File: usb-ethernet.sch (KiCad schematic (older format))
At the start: 17 parts

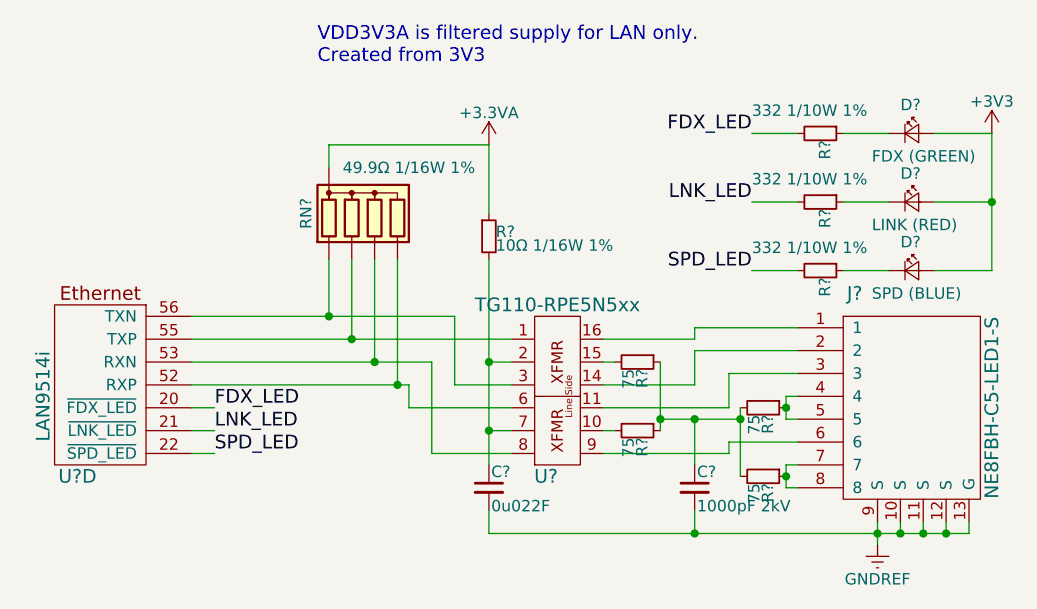
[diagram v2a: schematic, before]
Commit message: Updated footprint assignments
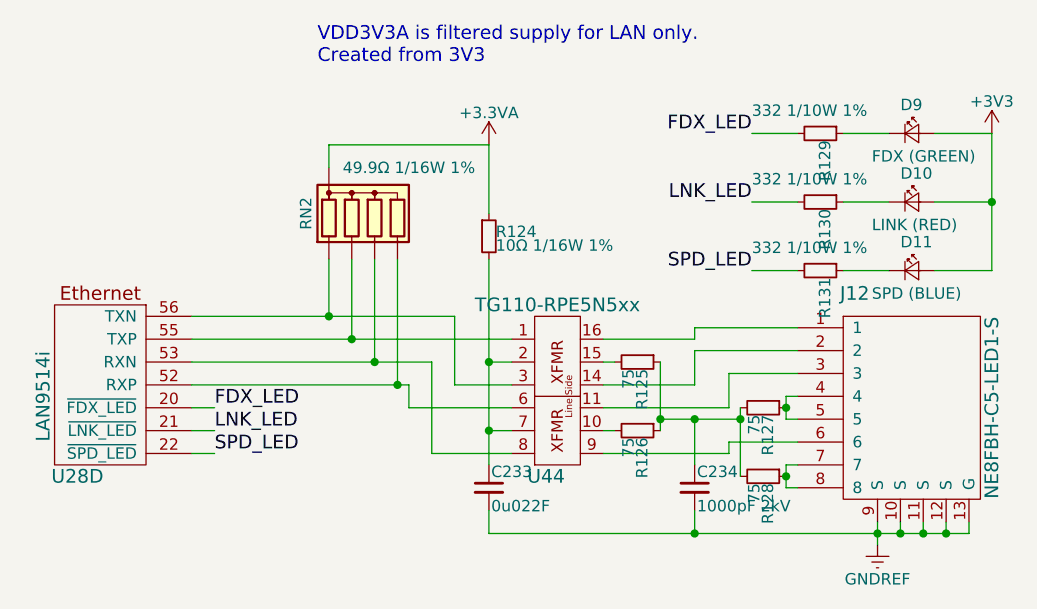
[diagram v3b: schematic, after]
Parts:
- C233, C234: renamed from C?; footprint Capacitors_SMD:C_0603_HandSoldering -> Capacitors_SMD:C_0603
- D10, D11, D9: renamed from D?; footprint (none) -> LEDs:LED_0603
- R124, R125, R126, R127, R128, R129, R130, R131: renamed from R?; footprint Capacitors_SMD:C_0603_HandSoldering -> Resistors_SMD:R_0603
- gave numbers to parts that had none: 4
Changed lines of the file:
@@
 P 3550 3750
 AR Path="/58DEDA35/5903ABC9" Ref="U?"  Part="4"
-AR Path="/58DEDA35/5903AB75/5903ABC9" Ref="U?"  Part="4"
-F 0 "U?" H 3650 3350 60  0000 C CNN
+AR Path="/58DEDA35/5903AB75/5903ABC9" Ref="U28"  Part="4"
+F 0 "U28" H 3650 3350 60  0000 C CNN
 F 1 "LAN9514i" V 3800 3700 60  0000 C CNN
 F 2 "Housings_DFN_QFN:QFN-64-1EP_9x9mm_Pitch0.5mm" H 4250 4250 60  0001 C CNN
@@
 $EndComp
 $Comp
-L TG110-RPE5N5xx U?
+L TG110-RPE5N5xx U44
 U 1 1 590032EB
 P 5550 3800
-F 0 "U?" H 5500 4150 60  0000 C CNN
+F 0 "U44" H 5500 4150 60  0000 C CNN
 F 1 "TG110-RPE5N5xx" H 5550 3400 60  0000 C CNN
 F 2 "" H 5050 4000 60  0001 C CNN
@@
 $EndComp
 $Comp
-L NE8FBH-C5-LED1-S J?
+L NE8FBH-C5-LED1-S J12
 U 1 1 5900332E
 P 7100 3800
-F 0 "J?" H 6850 4250 60  0000 C CNN
+F 0 "J12" H 6850 4250 60  0000 C CNN
 F 1 "NE8FBH-C5-LED1-S" V 7450 3750 60  0000 C CNN
 F 2 "" H 7000 3700 60  0001 C CNN
@@
 $EndComp
 $Comp
-L R_Small R?
+L R_Small R125
 U 1 1 5900376D
 P 5900 3650
-F 0 "R?" H 5930 3670 50  0000 L CNN
+F 0 "R125" H 5930 3670 50  0000 L CNN
 F 1 "75" H 5930 3610 50  0000 L CNN
-F 2 "Capacitors_SMD:C_0603_HandSoldering" H 5900 3650 50  0001 C CNN
+F 2 "Resistors_SMD:R_0603" H 5900 3650 50  0001 C CNN
 F 3 "" H 5900 3650 50  0001 C CNN
 	1    5900 3650
@@
 $EndComp
 $Comp
-L R_Small R?
+L R_Small R126
 U 1 1 590037C5
 P 5900 3950
-F 0 "R?" H 5930 3970 50  0000 L CNN
+F 0 "R126" H 5930 3970 50  0000 L CNN
 F 1 "75" H 5930 3910 50  0000 L CNN
-F 2 "Capacitors_SMD:C_0603_HandSoldering" H 5900 3950 50  0001 C CNN
+F 2 "Resistors_SMD:R_0603" H 5900 3950 50  0001 C CNN
 F 3 "" H 5900 3950 50  0001 C CNN
 	1    5900 3950
@@
 $EndComp
 $Comp
-L R_Small R?
+L R_Small R127
 U 1 1 5900382C
 P 6450 3850
-F 0 "R?" H 6480 3870 50  0000 L CNN
+F 0 "R127" H 6480 3870 50  0000 L CNN
 F 1 "75" H 6480 3810 50  0000 L CNN
-F 2 "Capacitors_SMD:C_0603_HandSoldering" H 6450 3850 50  0001 C CNN
+F 2 "Resistors_SMD:R_0603" H 6450 3850 50  0001 C CNN
 F 3 "" H 6450 3850 50  0001 C CNN
 	1    6450 3850
@@
 $EndComp
 $Comp
-L R_Small R?
+L R_Small R128
 U 1 1 59003855
 P 6450 4150
-F 0 "R?" H 6480 4170 50  0000 L CNN
+F 0 "R128" H 6480 4170 50  0000 L CNN
 F 1 "75" H 6480 4110 50  0000 L CNN
-F 2 "Capacitors_SMD:C_0603_HandSoldering" H 6450 4150 50  0001 C CNN
+F 2 "Resistors_SMD:R_0603" H 6450 4150 50  0001 C CNN
 F 3 "" H 6450 4150 50  0001 C CNN
 	1    6450 4150
@@
 $EndComp
 $Comp
-L C_Small C?
+L C_Small C234
 U 1 1 5900394D
 P 6150 4200
-F 0 "C?" H 6160 4270 50  0000 L CNN
+F 0 "C234" H 6160 4270 50  0000 L CNN
 F 1 "1000pF 2kV" H 6160 4120 50  0000 L CNN
-F 2 "Capacitors_SMD:C_0603_HandSoldering" H 6150 4200 50  0001 C CNN
+F 2 "Capacitors_SMD:C_0603" H 6150 4200 50  0001 C CNN
 F 3 "" H 6150 4200 50  0001 C CNN
 F 4 "0.00@0" H 6150 4200 60  0001 C CNN "Pricing"
@@
 $EndComp
 $Comp
-L GNDREF #PWR?
+L GNDREF #PWR0185
 U 1 1 59003AB4
 P 6950 4450
-F 0 "#PWR?" H 6950 4200 50  0001 C CNN
+F 0 "#PWR0185" H 6950 4200 50  0001 C CNN
 F 1 "GNDREF" H 6950 4300 50  0000 C CNN
 F 2 "" H 6950 4450 50  0001 C CNN
@@
 $EndComp
 $Comp
-L R_Small R?
+L R_Small R124
 U 1 1 59003EAC
 P 5250 3100
-F 0 "R?" H 5280 3120 50  0000 L CNN
+F 0 "R124" H 5280 3120 50  0000 L CNN
 F 1 "10Ω 1/16W 1%" H 5280 3060 50  0000 L CNN
-F 2 "Capacitors_SMD:C_0603_HandSoldering" H 5250 3100 50  0001 C CNN
+F 2 "Resistors_SMD:R_0603" H 5250 3100 50  0001 C CNN
 F 3 "" H 5250 3100 50  0001 C CNN
 F 4 "0.00@0" H 5250 3100 60  0001 C CNN "Pricing"
@@
 $EndComp
 $Comp
-L R_Network04 RN?
+L R_Network04 RN2
 U 1 1 5900455A
 P 4750 3000
-F 0 "RN?" V 4450 3000 50  0000 C CNN
+F 0 "RN2" V 4450 3000 50  0000 C CNN
 F 1 "49.9Ω 1/16W 1%" H 4900 3200 50  0000 C CNN
 F 2 "Resistors_THT:R_Array_SIP5" V 5025 3000 50  0001 C CNN
@@
 $EndComp
 $Comp
-L LED_Small D?
+L LED_Small D10
 U 1 1 59005A5F
 P 7100 2950
-F 0 "D?" H 7050 3075 50  0000 L CNN
+F 0 "D10" H 7050 3075 50  0000 L CNN
 F 1 "LINK (RED)" H 6925 2850 50  0000 L CNN
-F 2 "" V 7100 2950 50  0001 C CNN
+F 2 "LEDs:LED_0603" V 7100 2950 50  0001 C CNN
 F 3 "" V 7100 2950 50  0001 C CNN
 	1    7100 2950
@@
 $EndComp
 $Comp
-L LED_Small D?
+L LED_Small D11
 U 1 1 59005AF2
 P 7100 3250
-F 0 "D?" H 7050 3375 50  0000 L CNN
+F 0 "D11" H 7050 3375 50  0000 L CNN
 F 1 "SPD (BLUE)" H 6925 3150 50  0000 L CNN
-F 2 "" V 7100 3250 50  0001 C CNN
+F 2 "LEDs:LED_0603" V 7100 3250 50  0001 C CNN
 F 3 "" V 7100 3250 50  0001 C CNN
 	1    7100 3250
@@
 $EndComp
 $Comp
-L LED_Small D?
+L LED_Small D9
 U 1 1 59005B83
 P 7100 2650
-F 0 "D?" H 7050 2775 50  0000 L CNN
+F 0 "D9" H 7050 2775 50  0000 L CNN
 F 1 "FDX (GREEN)" H 6925 2550 50  0000 L CNN
-F 2 "" V 7100 2650 50  0001 C CNN
+F 2 "LEDs:LED_0603" V 7100 2650 50  0001 C CNN
 F 3 "" V 7100 2650 50  0001 C CNN
 F 4 "0.00@0" H 7100 2650 60  0001 C CNN "Pricing"
@@
 $EndComp
 $Comp
-L R_Small R?
+L R_Small R129
 U 1 1 59005DEC
 P 6700 2650
-F 0 "R?" H 6730 2670 50  0000 L CNN
+F 0 "R129" H 6730 2670 50  0000 L CNN
 F 1 "332 1/10W 1%" V 6600 2350 50  0000 L CNN
-F 2 "Capacitors_SMD:C_0603_HandSoldering" H 6700 2650 50  0001 C CNN
+F 2 "Resistors_SMD:R_0603" H 6700 2650 50  0001 C CNN
 F 3 "" H 6700 2650 50  0001 C CNN
 	1    6700 2650
@@
 $EndComp
 $Comp
-L R_Small R?
+L R_Small R130
 U 1 1 59005EDB
 P 6700 2950
-F 0 "R?" H 6730 2970 50  0000 L CNN
+F 0 "R130" H 6730 2970 50  0000 L CNN
 F 1 "332 1/10W 1%" V 6600 2650 50  0000 L CNN
-F 2 "Capacitors_SMD:C_0603_HandSoldering" H 6700 2950 50  0001 C CNN
+F 2 "Resistors_SMD:R_0603" H 6700 2950 50  0001 C CNN
 F 3 "" H 6700 2950 50  0001 C CNN
 	1    6700 2950
@@
 $EndComp
 $Comp
-L R_Small R?
+L R_Small R131
 U 1 1 59005F1A
 P 6700 3250
-F 0 "R?" H 6730 3270 50  0000 L CNN
+F 0 "R131" H 6730 3270 50  0000 L CNN
 F 1 "332 1/10W 1%" V 6600 2950 50  0000 L CNN
-F 2 "Capacitors_SMD:C_0603_HandSoldering" H 6700 3250 50  0001 C CNN
+F 2 "Resistors_SMD:R_0603" H 6700 3250 50  0001 C CNN
 F 3 "" H 6700 3250 50  0001 C CNN
 	1    6700 3250
@@
 $EndComp
 $Comp
-L +3V3 #PWR?
+L +3V3 #PWR0186
 U 1 1 590063C0
 P 7450 2650
-F 0 "#PWR?" H 7450 2500 50  0001 C CNN
+F 0 "#PWR0186" H 7450 2500 50  0001 C CNN
 F 1 "+3V3" H 7450 2790 50  0000 C CNN
 F 2 "" H 7450 2650 50  0001 C CNN
@@
 	6400 2950 6600 2950
 $Comp
-L C_Small C?
+L C_Small C233
 U 1 1 5901000F
 P 5250 4200
-F 0 "C?" H 5260 4270 50  0000 L CNN
+F 0 "C233" H 5260 4270 50  0000 L CNN
 F 1 "0u022F" H 5260 4120 50  0000 L CNN
-F 2 "Capacitors_SMD:C_0603_HandSoldering" H 5250 4200 50  0001 C CNN
+F 2 "Capacitors_SMD:C_0603" H 5250 4200 50  0001 C CNN
 F 3 "" H 5250 4200 50  0001 C CNN
 F 4 "0.00@0" H 5250 4200 60  0001 C CNN "Pricing"
@@
 Connection ~ 6150 4400
 $Comp
-L +3.3VA #PWR?
+L +3.3VA #PWR0187
 U 1 1 590123B2
 P 5250 2700
-F 0 "#PWR?" H 5250 2550 50  0001 C CNN
+F 0 "#PWR0187" H 5250 2550 50  0001 C CNN
 F 1 "+3.3VA" H 5250 2840 50  0000 C CNN
 F 2 "" H 5250 2700 50  0001 C CNN

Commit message: Started pcb layout, fixed some schematic issues
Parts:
- RN2: footprint Resistors_THT:R_Array_SIP5 -> Resistors_ThroughHole:R_Array_SIP5
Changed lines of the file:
@@
 F 0 "RN2" V 4450 3000 50  0000 C CNN
 F 1 "49.9Ω 1/16W 1%" H 4900 3200 50  0000 C CNN
-F 2 "Resistors_THT:R_Array_SIP5" V 5025 3000 50  0001 C CNN
+F 2 "Resistors_ThroughHole:R_Array_SIP5" V 5025 3000 50  0001 C CNN
 F 3 "" H 4750 3000 50  0001 C CNN
 	1    4750 3000

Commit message: Added all missing nonstandard footprints
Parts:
- J12: footprint (none) -> SW-Neutrik:NE8FBH-C5-LED1-S
- U44: footprint (none) -> SW-HALO:HALO-Ultra-POE-XFMR
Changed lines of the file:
@@
 F 0 "U44" H 5500 4150 60  0000 C CNN
 F 1 "TG110-RPE5N5xx" H 5550 3400 60  0000 C CNN
-F 2 "" H 5050 4000 60  0001 C CNN
+F 2 "SW-HALO:HALO-Ultra-POE-XFMR" H 5050 4000 60  0001 C CNN
 F 3 "http://www.mouser.com/ds/2/706/discrete-ultrapoe-100baset-523855.pdf" H 5550 4600 60  0001 C CNN
 F 4 "0.00@0" H 5550 4750 60  0001 C CNN "Pricing"
@@
 F 0 "J12" H 6850 4250 60  0000 C CNN
 F 1 "NE8FBH-C5-LED1-S" V 7450 3750 60  0000 C CNN
-F 2 "" H 7000 3700 60  0001 C CNN
+F 2 "SW-Neutrik:NE8FBH-C5-LED1-S" H 7000 3700 60  0001 C CNN
 F 3 "http://www.neutrik.us/zoolu-website/media/download/13417/Drawing+NE8FBH-C5-LED1-S" H 7100 4950 60  0001 C CNN
-F 4 "0.00@0" H 7100 5500 60  0001 C CNN "Pricing"
-F 5 "Horizontal PCB mount RJ45 receptacle, CAT5e, shielded, two light pipes for SMD-LEDs, B-Series cutout with latch lock, max. panel thickness 3 mm" H 6900 5100 60  0001 C CNN "Characteristics"
+F 4 "Horizontal PCB mount RJ45 receptacle, CAT5e, shielded, two light pipes for SMD-LEDs, B-Series cutout with latch lock, max. panel thickness 3 mm" H 6900 5100 60  0001 C CNN "Characteristics"
+F 5 "Neutrik" H 7000 5200 60  0001 C CNN "Manufacturer"
 F 6 "Horizontal PCB mount RJ45 receptacle, CAT5e, shielded, two light pipes for SMD-LEDs, B-Series cutout with latch lock, max. panel thickness 3 mm" H 7100 5300 60  0001 C CNN "Description"
-F 7 "Neutrik" H 7000 5200 60  0001 C CNN "Manufacturer"
+F 7 "0.00@0" H 7100 5500 60  0001 C CNN "Pricing"
 	1    7100 3800
 	1    0    0    -1

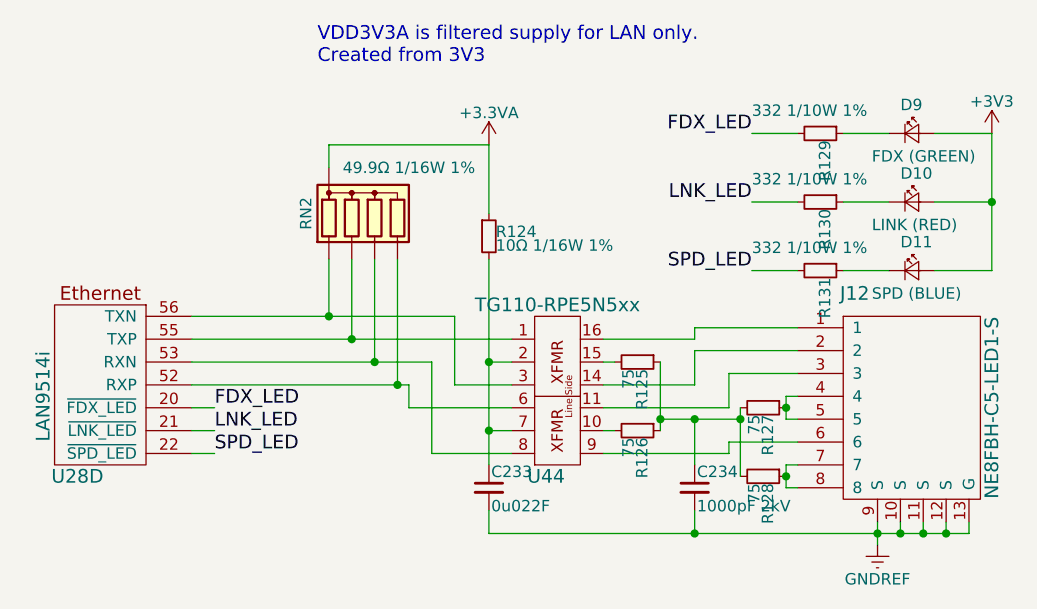
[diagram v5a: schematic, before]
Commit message: Final edits of resistor networks and footprints
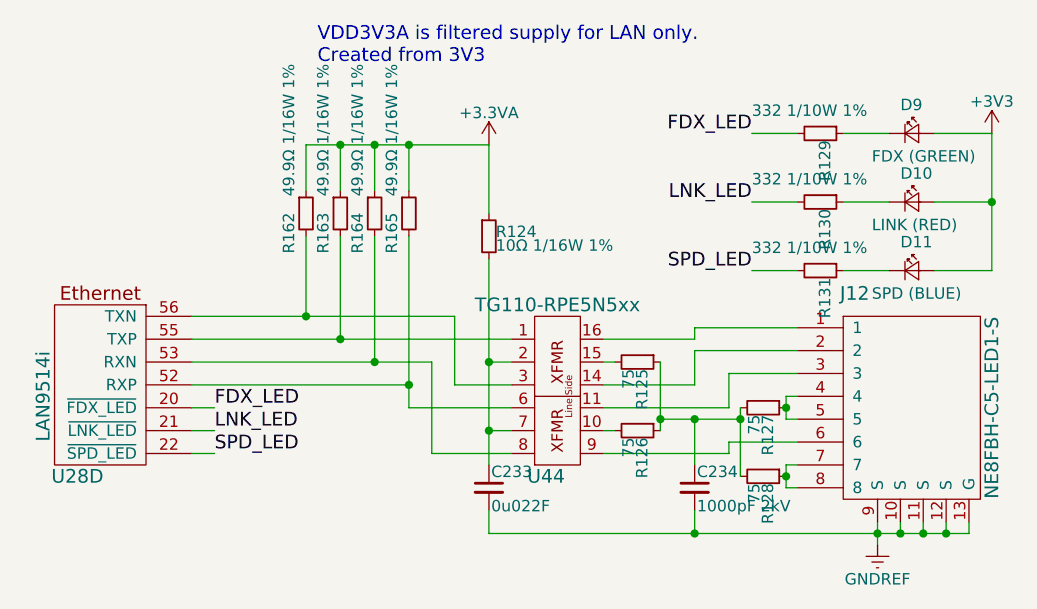
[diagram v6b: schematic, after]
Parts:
- removed RN2: 49.9Ω 1/16W 1%, Resistors_ThroughHole:R_Array_SIP5, symbol R_Network04
- added R162, R163, R164, R165: 49.9Ω 1/16W 1%, Resistors_SMD:R_0603, symbol R_Small
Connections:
- net +3.3VA: now also R162.1, R163.1, R164.1, R165.1
- net at U28.55 (TXP), U44.1: now also R163.2
- net at U28.56 (TXN), U44.3: now also R162.2
- net at U28.52 (RXP), U44.6: now also R165.2
- net at U28.53 (RXN), U44.8: now also R164.2
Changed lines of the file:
@@
-$EndComp
-$Comp
-L R_Network04 RN2
-U 1 1 5900455A
-P 4750 3000
-F 0 "RN2" V 4450 3000 50  0000 C CNN
-F 1 "49.9Ω 1/16W 1%" H 4900 3200 50  0000 C CNN
-F 2 "Resistors_ThroughHole:R_Array_SIP5" V 5025 3000 50  0001 C CNN
-F 3 "" H 4750 3000 50  0001 C CNN
-	1    4750 3000
-	1    0    0    -1
 $EndComp
 $Comp
@@
 	3950 3450 5100 3450
 Wire Wire Line
-	5350 3850 4900 3850
-Wire Wire Line
-	4900 3850 4900 3750
+	4900 3850 5350 3850
+Wire Wire Line
+	4900 3100 4900 3850
 Wire Wire Line
 	4900 3750 3950 3750
@@
 Wire Wire Line
 	5000 3650 3950 3650
-Wire Wire Line
-	4850 3200 4850 3750
-Connection ~ 4850 3750
-Wire Wire Line
-	4750 3200 4750 3650
+Connection ~ 4900 3750
+Wire Wire Line
+	4750 3100 4750 3650
 Connection ~ 4750 3650
 Wire Wire Line
-	4650 3200 4650 3550
-Connection ~ 4650 3550
-Wire Wire Line
-	4550 3200 4550 3450
-Connection ~ 4550 3450
+	4600 3100 4600 3550
+Connection ~ 4600 3550
+Wire Wire Line
+	4450 3100 4450 3450
+Connection ~ 4450 3450
 Wire Wire Line
 	5250 2700 5250 3000
 Wire Wire Line
-	4550 2700 5250 2700
-Wire Wire Line
-	4550 2700 4550 2800
+	4450 2700 5250 2700
+Wire Wire Line
+	4600 2700 4600 2900
 Wire Wire Line
 	7450 3250 7200 3250
@@
 Text Notes 4500 2350 0    60   ~ 0
 VDD3V3A is filtered supply for LAN only.\nCreated from 3V3
+$Comp
+L R_Small R162
+U 1 1 591AD852
+P 4450 3000
+F 0 "R162" V 4375 2825 50  0000 L CNN
+F 1 "49.9Ω 1/16W 1%" V 4375 3075 50  0000 L CNN
+F 2 "Resistors_SMD:R_0603" H 4450 3000 50  0001 C CNN
+F 3 "" H 4450 3000 50  0001 C CNN
+	1    4450 3000
+	1    0    0    -1
+$EndComp
+$Comp
+L R_Small R163
+U 1 1 591ADAD2
+P 4600 3000
+F 0 "R163" V 4525 2825 50  0000 L CNN
+F 1 "49.9Ω 1/16W 1%" V 4525 3075 50  0000 L CNN
+F 2 "Resistors_SMD:R_0603" H 4600 3000 50  0001 C CNN
+F 3 "" H 4600 3000 50  0001 C CNN
+	1    4600 3000
+	1    0    0    -1
+$EndComp
+$Comp
+L R_Small R164
+U 1 1 591ADB16
+P 4750 3000
+F 0 "R164" V 4675 2825 50  0000 L CNN
+F 1 "49.9Ω 1/16W 1%" V 4675 3075 50  0000 L CNN
+F 2 "Resistors_SMD:R_0603" H 4750 3000 50  0001 C CNN
+F 3 "" H 4750 3000 50  0001 C CNN
+	1    4750 3000
+	1    0    0    -1
+$EndComp
+$Comp
+L R_Small R165
+U 1 1 591ADB5D
+P 4900 3000
+F 0 "R165" V 4825 2825 50  0000 L CNN
+F 1 "49.9Ω 1/16W 1%" V 4825 3075 50  0000 L CNN
+F 2 "Resistors_SMD:R_0603" H 4900 3000 50  0001 C CNN
+F 3 "" H 4900 3000 50  0001 C CNN
+	1    4900 3000
+	1    0    0    -1
+$EndComp
+Wire Wire Line
+	4450 2900 4450 2700
+Connection ~ 4600 2700
+Wire Wire Line
+	4750 2900 4750 2700
+Connection ~ 4750 2700
+Wire Wire Line
+	4900 2900 4900 2700
+Connection ~ 4900 2700
 $EndSCHEMATC

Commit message: More work on pcb layout
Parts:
- R124, R125, R126, R127, R128, R162, R163, R164, R165: footprint Resistors_SMD:R_0603 -> Resistors_SMD:R_0402_NoSilk
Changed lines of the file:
@@
 F 0 "R125" H 5930 3670 50  0000 L CNN
 F 1 "75" H 5930 3610 50  0000 L CNN
-F 2 "Resistors_SMD:R_0603" H 5900 3650 50  0001 C CNN
+F 2 "Resistors_SMD:R_0402_NoSilk" H 5900 3650 50  0001 C CNN
 F 3 "" H 5900 3650 50  0001 C CNN
 	1    5900 3650
@@
 F 0 "R126" H 5930 3970 50  0000 L CNN
 F 1 "75" H 5930 3910 50  0000 L CNN
-F 2 "Resistors_SMD:R_0603" H 5900 3950 50  0001 C CNN
+F 2 "Resistors_SMD:R_0402_NoSilk" H 5900 3950 50  0001 C CNN
 F 3 "" H 5900 3950 50  0001 C CNN
 	1    5900 3950
@@
 F 0 "R127" H 6480 3870 50  0000 L CNN
 F 1 "75" H 6480 3810 50  0000 L CNN
-F 2 "Resistors_SMD:R_0603" H 6450 3850 50  0001 C CNN
+F 2 "Resistors_SMD:R_0402_NoSilk" H 6450 3850 50  0001 C CNN
 F 3 "" H 6450 3850 50  0001 C CNN
 	1    6450 3850
@@
 F 0 "R128" H 6480 4170 50  0000 L CNN
 F 1 "75" H 6480 4110 50  0000 L CNN
-F 2 "Resistors_SMD:R_0603" H 6450 4150 50  0001 C CNN
+F 2 "Resistors_SMD:R_0402_NoSilk" H 6450 4150 50  0001 C CNN
 F 3 "" H 6450 4150 50  0001 C CNN
 	1    6450 4150
@@
 F 0 "R124" H 5280 3120 50  0000 L CNN
 F 1 "10Ω 1/16W 1%" H 5280 3060 50  0000 L CNN
-F 2 "Resistors_SMD:R_0603" H 5250 3100 50  0001 C CNN
+F 2 "Resistors_SMD:R_0402_NoSilk" H 5250 3100 50  0001 C CNN
 F 3 "" H 5250 3100 50  0001 C CNN
 F 4 "0.00@0" H 5250 3100 60  0001 C CNN "Pricing"
@@
 F 0 "R162" V 4375 2825 50  0000 L CNN
 F 1 "49.9Ω 1/16W 1%" V 4375 3075 50  0000 L CNN
-F 2 "Resistors_SMD:R_0603" H 4450 3000 50  0001 C CNN
+F 2 "Resistors_SMD:R_0402_NoSilk" H 4450 3000 50  0001 C CNN
 F 3 "" H 4450 3000 50  0001 C CNN
 	1    4450 3000
@@
 F 0 "R163" V 4525 2825 50  0000 L CNN
 F 1 "49.9Ω 1/16W 1%" V 4525 3075 50  0000 L CNN
-F 2 "Resistors_SMD:R_0603" H 4600 3000 50  0001 C CNN
+F 2 "Resistors_SMD:R_0402_NoSilk" H 4600 3000 50  0001 C CNN
 F 3 "" H 4600 3000 50  0001 C CNN
 	1    4600 3000
@@
 F 0 "R164" V 4675 2825 50  0000 L CNN
 F 1 "49.9Ω 1/16W 1%" V 4675 3075 50  0000 L CNN
-F 2 "Resistors_SMD:R_0603" H 4750 3000 50  0001 C CNN
+F 2 "Resistors_SMD:R_0402_NoSilk" H 4750 3000 50  0001 C CNN
 F 3 "" H 4750 3000 50  0001 C CNN
 	1    4750 3000
@@
 F 0 "R165" V 4825 2825 50  0000 L CNN
 F 1 "49.9Ω 1/16W 1%" V 4825 3075 50  0000 L CNN
-F 2 "Resistors_SMD:R_0603" H 4900 3000 50  0001 C CNN
+F 2 "Resistors_SMD:R_0402_NoSilk" H 4900 3000 50  0001 C CNN
 F 3 "" H 4900 3000 50  0001 C CNN
 	1    4900 3000
